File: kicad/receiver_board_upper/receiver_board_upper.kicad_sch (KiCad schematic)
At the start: 13 parts, among them J1 Battery Conn, J2 Motor 1, J3 Motor 2, Q1 FQP27P06, SW1 On/Off, SW2 Pair/Direction, U1 2S BMS, U2 5V Buck, U4 Dual H Bridge, U5 ESP32-C3-SuperMini

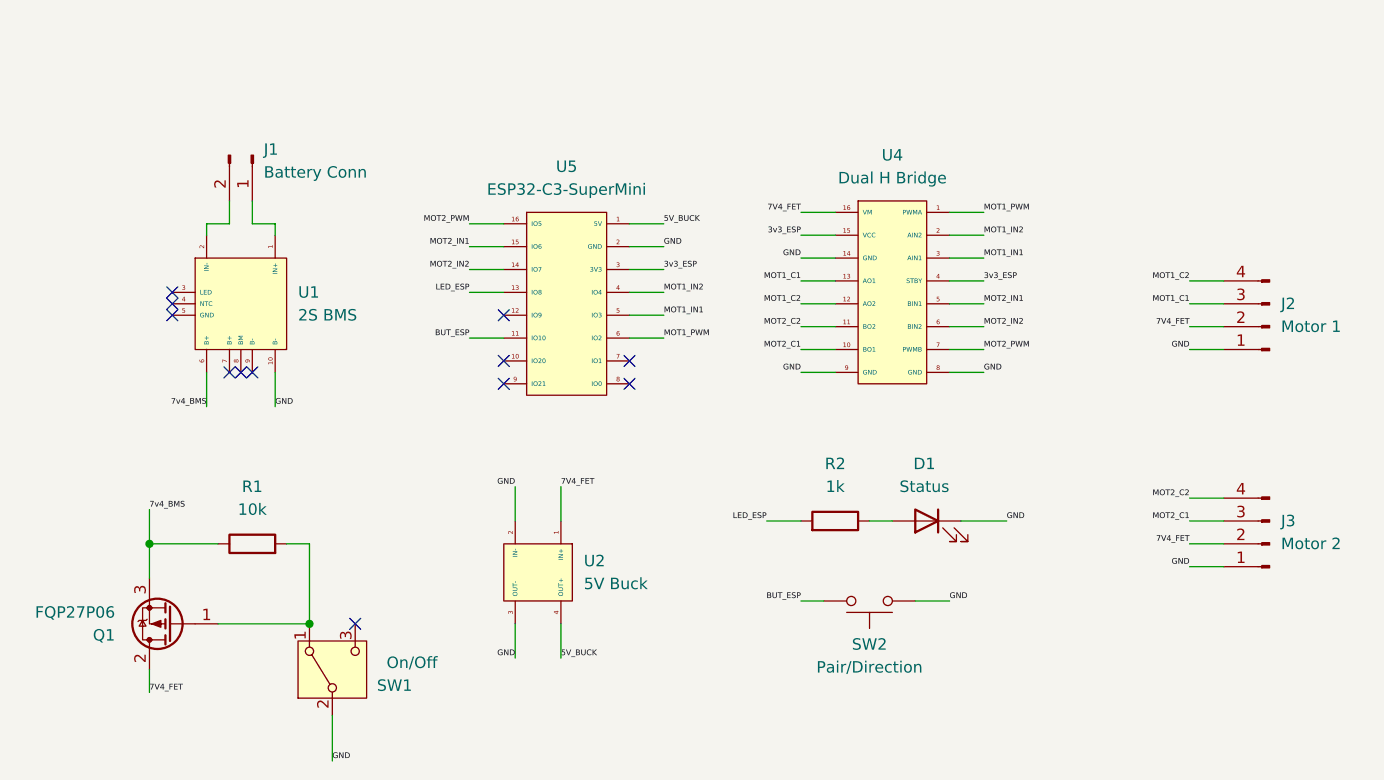
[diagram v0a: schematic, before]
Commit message: Split receiver into two-board design for PF battery box fit
Divide receiver into upper and lower PCBs to meet physical constraints
of Lego Power Functions 8x4 stud battery box housing.

Lower board (receiver_board_lower):
- 2S BMS with USB-C charging
- MP1584EN buck converter (8.4V → 5V)
- FQP27P06 P-FET power switching
- Power distribution to upper board

Upper board (receiver_board_upper):
- ESP32-C3-SuperMini
- TB6612FNG dual H-bridge motor driver
- 2x JST-XH motor connectors (4-pin, Lego PF compatible)
- Status LED, pairing button, and SPDT on/off switch
- Control logic and motor outputs

Renamed receiver_board to receiver_board_upper for clarity.

TODO: Clean up nets between boards, design board-to-board connector
(power rails: 7V4_FET, GND, 5V; signals: FET gate control from switch).

Co-Authored-By: Claude Sonnet 4.5 <noreply@anthropic.com>
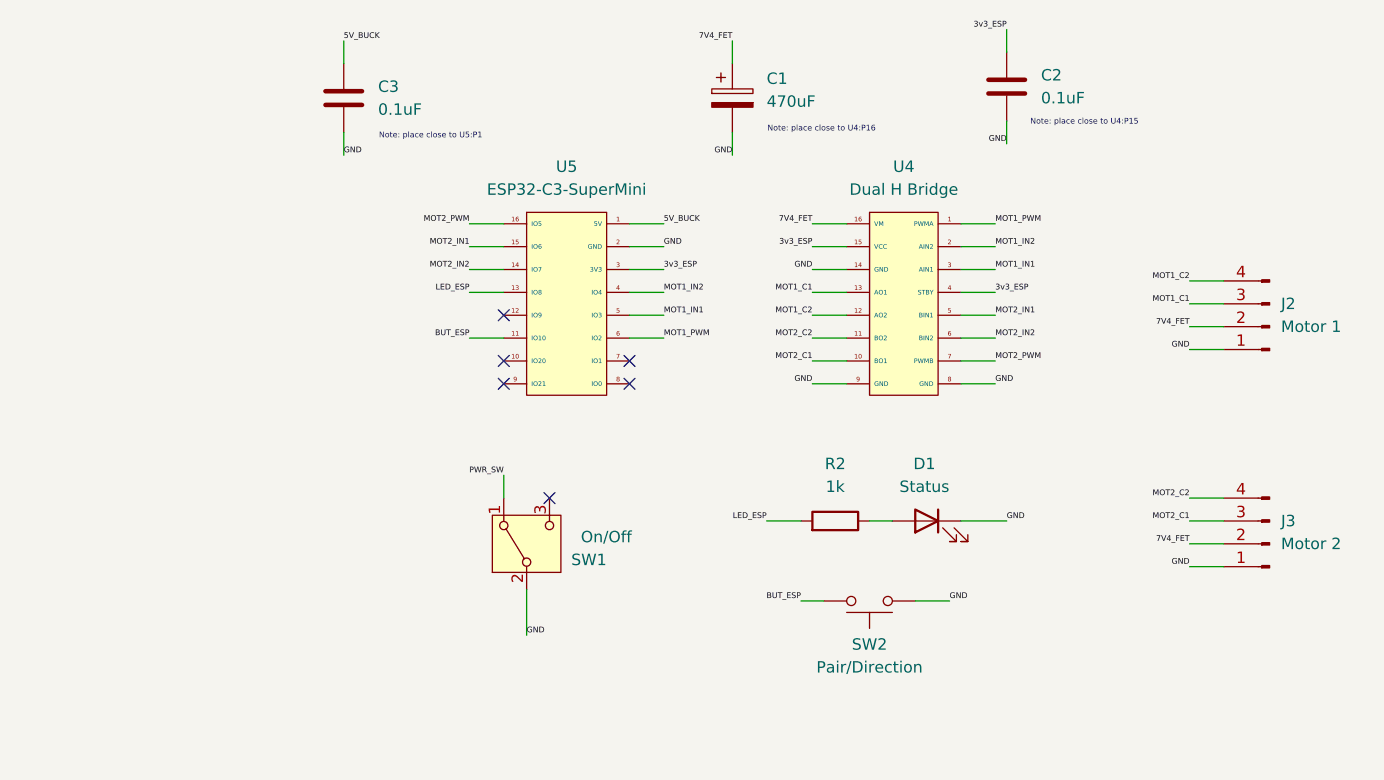
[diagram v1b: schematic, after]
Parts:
- removed J1: Battery Conn, Connector_PinHeader_2.54mm:PinHeader_1x02_P2.54mm_Horizontal, symbol Connector:Conn_01x02_Pin
- removed Q1: FQP27P06, Package_TO_SOT_THT:TO-220-3_Vertical, symbol Transistor_FET:FQP27P06
- removed R1: 10k, Resistor_THT:R_Axial_DIN0207_L6.3mm_D2.5mm_P7.62mm_Horizontal, symbol Device:R
- removed U1: 2S BMS, symbol ESP32_Lego_PF:2S_BMS
- removed U2: 5V Buck, symbol ESP32_Lego_PF:MP1584EN
- added C1: 470uF, symbol Device:C_Polarized
- added C2, C3: 0.1uF, symbol Device:C
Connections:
- net 3v3_ESP: now also C2.1
- net 5V_BUCK: now also C3.1
- net 7V4_FET: now also C1.1
- net GND: now also C1.2, C2.2, C3.2
- net PWR_SW: now reaches SW1.1 (A)
- no-connect marks 12 -> 6
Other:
- note added: "Note: place close to U4:P15"
- note added: "Note: place close to U4:P16"
- note added: "Note: place close to U5:P1"
- moved on the sheet: SW1, U4
